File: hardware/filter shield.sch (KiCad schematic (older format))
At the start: 9 parts, among them J1 Screw_Terminal_01x03, J2 Screw_Terminal_01x03, J3 TR switch Connector, J6 Screw_Terminal_01x03, J7 Radioberry Connector, J8 BPF Connector, J9 LPF Connector, U1 BOB-12009

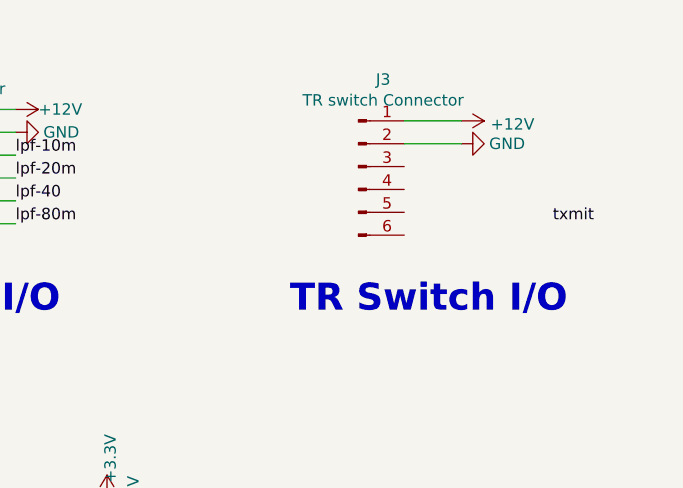
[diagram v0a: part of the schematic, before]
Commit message: tr switch circuit added
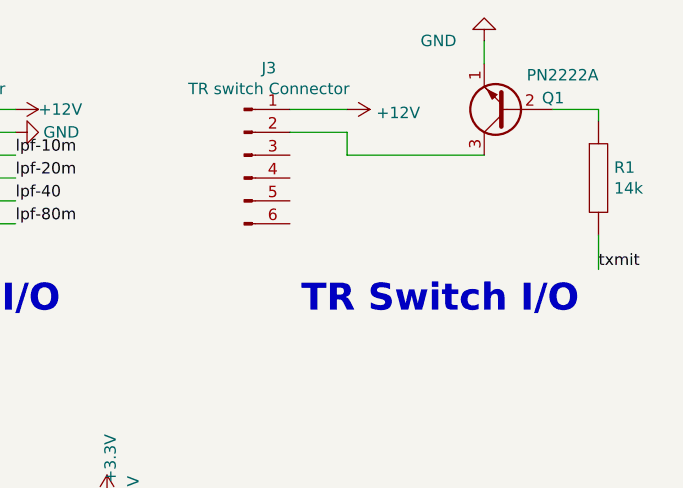
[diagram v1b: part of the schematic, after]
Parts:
- added Q1: PN2222A, Package_TO_SOT_THT:TO-92_Inline, symbol Transistor_BJT:PN2222A
- added R1: 14k, Resistor_THT:R_Axial_DIN0204_L3.6mm_D1.6mm_P7.62mm_Horizontal, symbol pspice:R
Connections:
- net GND: now also Q1.1 (E); no longer J3.2 (Pin_2)
- net txmit: now also R1.2
- new net: Q1.2 (B), R1.1
- new net: J3.2 (Pin_2), Q1.3 (C)
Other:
- moved on the sheet: J3
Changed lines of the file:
@@
 Text Label 5600 4100 0    50   ~ 0
 ptt
-Text Label 10300 1500 0    50   ~ 0
+Text Label 10500 1700 0    50   ~ 0
 txmit
 Text Label 5800 1050 0    50   ~ 0
@@
 L power:GND #PWR0129
 U 1 1 5E57ED2C
-P 9900 1150
-F 0 "#PWR0129" H 9900 900 50  0001 C CNN
-F 1 "GND" V 9900 950 50  0000 C CNN
-F 2 "" H 9900 1150 50  0001 C CNN
-F 3 "" H 9900 1150 50  0001 C CNN
-	1    9900 1150
-	0    -1   -1   0
+P 10000 700
+F 0 "#PWR0129" H 10000 450 50  0001 C CNN
+F 1 "GND" H 10200 700 50  0000 C CNN
+F 2 "" H 10000 700 50  0001 C CNN
+F 3 "" H 10000 700 50  0001 C CNN
+	1    10000 700
+	-1   0    0    1
 $EndComp
 Wire Wire Line
@@
 L power:+12V #PWR0103
 U 1 1 5E5083D9
-P 9900 1050
-F 0 "#PWR0103" H 9900 900 50  0001 C CNN
-F 1 "+12V" V 9915 1178 50  0000 L CNN
-F 2 "" H 9900 1050 50  0001 C CNN
-F 3 "" H 9900 1050 50  0001 C CNN
-	1    9900 1050
+P 9400 1000
+F 0 "#PWR0103" H 9400 850 50  0001 C CNN
+F 1 "+12V" V 9415 1128 50  0000 L CNN
+F 2 "" H 9400 1000 50  0001 C CNN
+F 3 "" H 9400 1000 50  0001 C CNN
+	1    9400 1000
 	0    1    1    0
 $EndComp
@@
 L Connector:Conn_01x06_Male J3
 U 1 1 5E5186BE
-P 9450 1250
-F 0 "J3" H 9558 1631 50  0000 C CNN
-F 1 "TR switch Connector" H 9558 1540 50  0000 C CNN
-F 2 "Connector_PinHeader_2.54mm:PinHeader_1x06_P2.54mm_Vertical" H 9450 1250 50  0001 C CNN
-F 3 "~" H 9450 1250 50  0001 C CNN
-	1    9450 1250
+P 8950 1200
+F 0 "J3" H 9058 1581 50  0000 C CNN
+F 1 "TR switch Connector" H 9058 1490 50  0000 C CNN
+F 2 "Connector_PinHeader_2.54mm:PinHeader_1x06_P2.54mm_Vertical" H 8950 1200 50  0001 C CNN
+F 3 "~" H 8950 1200 50  0001 C CNN
+	1    8950 1200
 	1    0    0    -1
 $EndComp
@@
 	5850 1550 5600 1550
 Wire Wire Line
-	9900 1050 9650 1050
-Wire Wire Line
-	9900 1150 9650 1150
+	9400 1000 9150 1000
+Wire Wire Line
+	9400 1100 9150 1100
 Text Notes 750  1900 0    118  ~ 24
 Power Inputs
@@
 Text Notes 7500 1900 0    118  ~ 24
 LPF I/O
-Text Notes 9150 1900 0    118  ~ 24
+Text Notes 9200 1900 0    118  ~ 24
 TR Switch I/O
 Text Notes 950  4500 0    118  ~ 24
@@
 Wire Wire Line
 	7750 4150 7400 4150
+$Comp
+L pspice:R R1
+U 1 1 5E4E14AD
+P 10500 1300
+F 0 "R1" H 10568 1346 50  0000 L CNN
+F 1 "14k" H 10568 1255 50  0000 L CNN
+F 2 "Resistor_THT:R_Axial_DIN0204_L3.6mm_D1.6mm_P7.62mm_Horizontal" H 10500 1300 50  0001 C CNN
+F 3 "~" H 10500 1300 50  0001 C CNN
+	1    10500 1300
+	1    0    0    -1
+$EndComp
+$Comp
+L Transistor_BJT:PN2222A Q1
+U 1 1 5E4E27AE
+P 10100 1000
+F 0 "Q1" H 9850 950 50  0000 L CNN
+F 1 "PN2222A" H 9700 850 50  0000 L CNN
+F 2 "Package_TO_SOT_THT:TO-92_Inline" H 10300 925 50  0001 L CIN
+F 3 "http://www.fairchildsemi.com/ds/PN/PN2222A.pdf" H 10100 1000 50  0001 L CNN
+	1    10100 1000
+	-1   0    0    1
+$EndComp
+Wire Wire Line
+	10000 700  10000 800
+Wire Wire Line
+	10500 1050 10500 1000
+Wire Wire Line
+	10500 1000 10300 1000
+Wire Wire Line
+	10500 1700 10500 1550
+Wire Wire Line
+	10000 1200 9400 1200
+Wire Wire Line
+	9400 1200 9400 1100
 $EndSCHEMATC

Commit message: Small corrections
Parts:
- added Q2: PN2222A, Package_TO_SOT_THT:TO-92_Inline, symbol Transistor_BJT:PN2222A
- added R2: 14k, Resistor_THT:R_Axial_DIN0204_L3.6mm_D1.6mm_P7.62mm_Horizontal, symbol pspice:R
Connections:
- net GND: now also J3.3 (Pin_3), J3.5 (Pin_5), Q2.1 (E)
- net pa: now reaches A1.9 (D6)
- net pa: now also R2.2
- net at J3.4 (Pin_4): now also Q2.3 (C)
- new net: Q2.2 (B), R2.1
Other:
- note added: "TR Switch-PA I/O"
- note removed: "TR Switch I/O"
- moved on the sheet: R1
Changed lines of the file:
@@
 Text Label 5600 4100 0    50   ~ 0
 ptt
-Text Label 10500 1700 0    50   ~ 0
+Text Label 10800 1000 0    50   ~ 0
 txmit
 Text Label 5800 1050 0    50   ~ 0
@@
 Text Notes 7500 1900 0    118  ~ 24
 LPF I/O
-Text Notes 9200 1900 0    118  ~ 24
-TR Switch I/O
+Text Notes 9200 2200 0    118  ~ 24
+TR Switch-PA I/O
 Text Notes 950  4500 0    118  ~ 24
 PA power
@@
 L pspice:R R1
 U 1 1 5E4E14AD
-P 10500 1300
-F 0 "R1" H 10568 1346 50  0000 L CNN
-F 1 "14k" H 10568 1255 50  0000 L CNN
-F 2 "Resistor_THT:R_Axial_DIN0204_L3.6mm_D1.6mm_P7.62mm_Horizontal" H 10500 1300 50  0001 C CNN
-F 3 "~" H 10500 1300 50  0001 C CNN
-	1    10500 1300
-	1    0    0    -1
+P 10550 1000
+F 0 "R1" H 10618 1046 50  0000 L CNN
+F 1 "14k" H 10618 955 50  0000 L CNN
+F 2 "Resistor_THT:R_Axial_DIN0204_L3.6mm_D1.6mm_P7.62mm_Horizontal" H 10550 1000 50  0001 C CNN
+F 3 "~" H 10550 1000 50  0001 C CNN
+	1    10550 1000
+	0    -1   -1   0
 $EndComp
 $Comp
@@
 	10000 700  10000 800
 Wire Wire Line
-	10500 1050 10500 1000
-Wire Wire Line
-	10500 1000 10300 1000
-Wire Wire Line
-	10500 1700 10500 1550
-Wire Wire Line
 	10000 1200 9400 1200
 Wire Wire Line
 	9400 1200 9400 1100
+$Comp
+L power:GND #PWR0120
+U 1 1 5E50D80E
+P 10000 1350
+F 0 "#PWR0120" H 10000 1100 50  0001 C CNN
+F 1 "GND" H 10200 1350 50  0000 C CNN
+F 2 "" H 10000 1350 50  0001 C CNN
+F 3 "" H 10000 1350 50  0001 C CNN
+	1    10000 1350
+	-1   0    0    1
+$EndComp
+$Comp
+L pspice:R R2
+U 1 1 5E50D819
+P 10550 1650
+F 0 "R2" H 10618 1696 50  0000 L CNN
+F 1 "14k" H 10618 1605 50  0000 L CNN
+F 2 "Resistor_THT:R_Axial_DIN0204_L3.6mm_D1.6mm_P7.62mm_Horizontal" H 10550 1650 50  0001 C CNN
+F 3 "~" H 10550 1650 50  0001 C CNN
+	1    10550 1650
+	0    -1   -1   0
+$EndComp
+$Comp
+L Transistor_BJT:PN2222A Q2
+U 1 1 5E50D823
+P 10100 1650
+F 0 "Q2" H 9850 1600 50  0000 L CNN
+F 1 "PN2222A" H 9700 1500 50  0000 L CNN
+F 2 "Package_TO_SOT_THT:TO-92_Inline" H 10300 1575 50  0001 L CIN
+F 3 "http://www.fairchildsemi.com/ds/PN/PN2222A.pdf" H 10100 1650 50  0001 L CNN
+	1    10100 1650
+	-1   0    0    1
+$EndComp
+Wire Wire Line
+	10000 1350 10000 1450
+Wire Wire Line
+	10000 1850 9400 1850
+Text Label 7400 4050 0    50   ~ 0
+pa
+Text Label 10800 1650 0    50   ~ 0
+pa
+Wire Wire Line
+	7400 4050 7750 4050
+Wire Wire Line
+	9400 1850 9400 1300
+Wire Wire Line
+	9400 1300 9150 1300
+$Comp
+L power:GND #PWR0121
+U 1 1 5E53E548
+P 9150 1400
+F 0 "#PWR0121" H 9150 1150 50  0001 C CNN
+F 1 "GND" V 9150 1200 50  0000 C CNN
+F 2 "" H 9150 1400 50  0001 C CNN
+F 3 "" H 9150 1400 50  0001 C CNN
+	1    9150 1400
+	0    -1   -1   0
+$EndComp
+$Comp
+L power:GND #PWR0122
+U 1 1 5E540C7C
+P 9150 1200
+F 0 "#PWR0122" H 9150 950 50  0001 C CNN
+F 1 "GND" V 9150 1000 50  0000 C CNN
+F 2 "" H 9150 1200 50  0001 C CNN
+F 3 "" H 9150 1200 50  0001 C CNN
+	1    9150 1200
+	0    -1   -1   0
+$EndComp
 $EndSCHEMATC

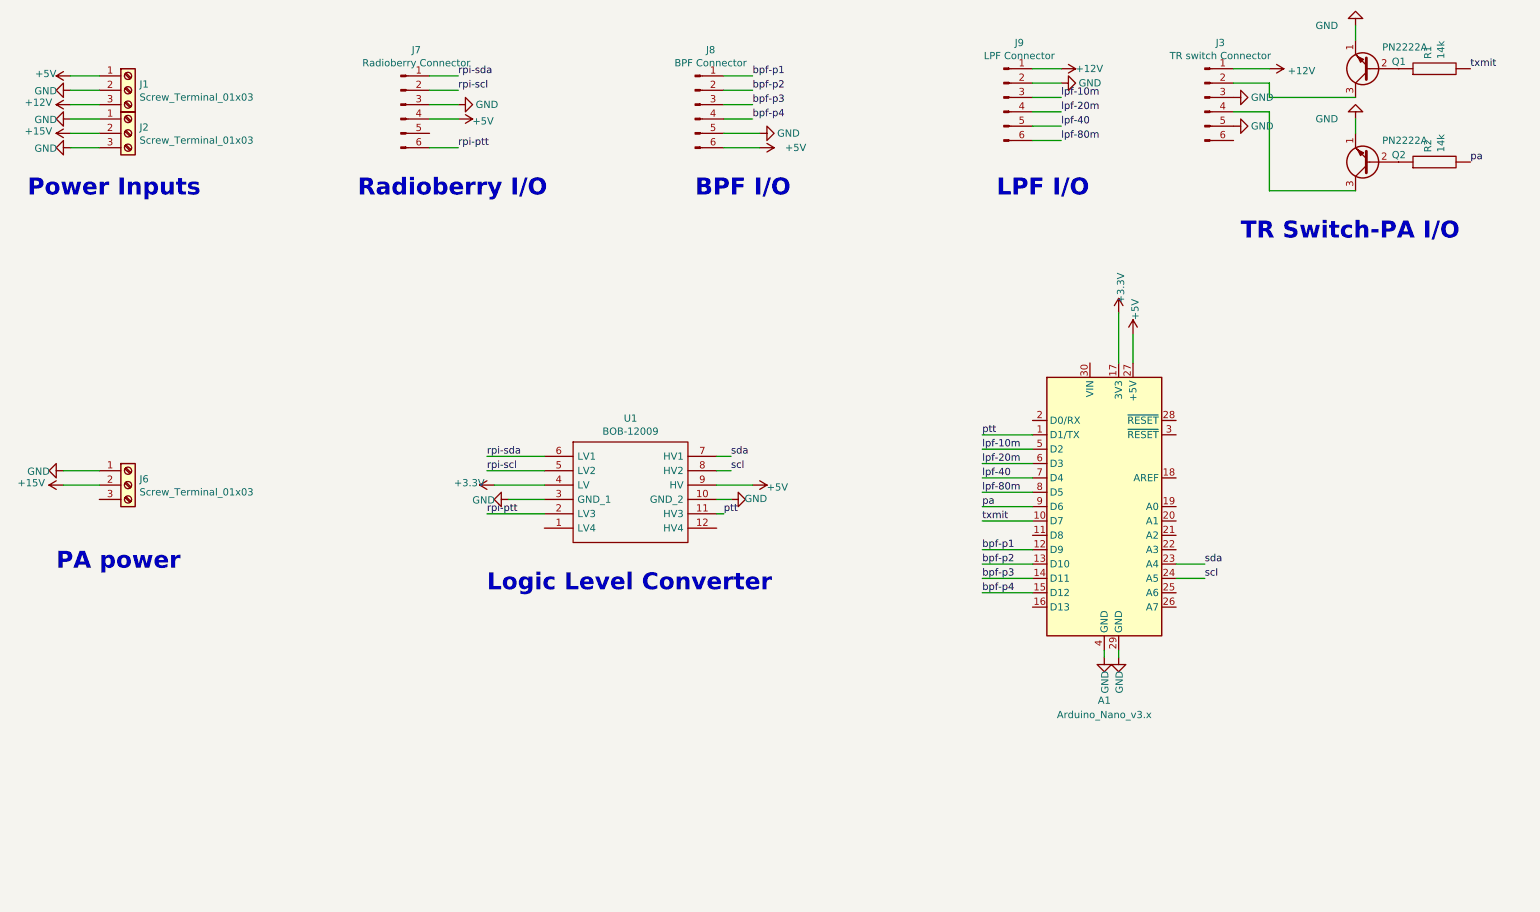
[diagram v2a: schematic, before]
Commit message: Revised circuit to meet lpf protocol. Added futur expansion i/o over analog pins
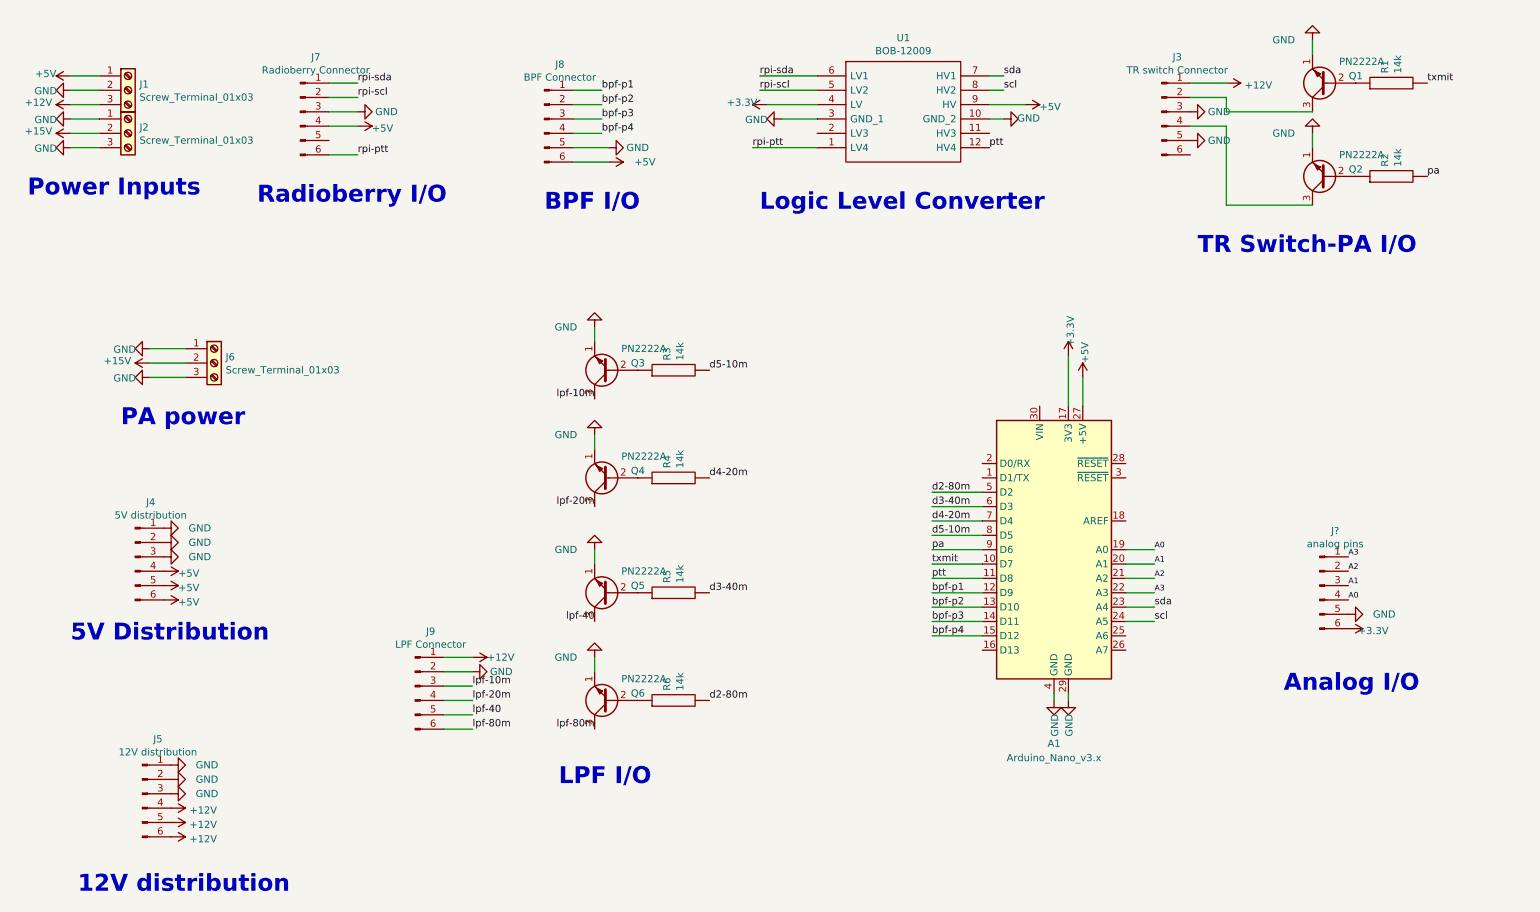
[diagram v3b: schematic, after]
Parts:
- added J4: 5V distribution, Connector_PinHeader_2.54mm:PinHeader_1x06_P2.54mm_Vertical, symbol Connector:Conn_01x06_Male
- added J5: 12V distribution, Connector_PinHeader_2.54mm:PinHeader_1x06_P2.54mm_Vertical, symbol Connector:Conn_01x06_Male
- added J?: analog pins, Connector_PinHeader_2.54mm:PinHeader_1x06_P2.54mm_Vertical, symbol Connector:Conn_01x06_Male
- added Q3, Q4, Q5, Q6: PN2222A, Package_TO_SOT_THT:TO-92_Inline, symbol Transistor_BJT:PN2222A
- added R3, R4, R5, R6: 14k, Resistor_THT:R_Axial_DIN0204_L3.6mm_D1.6mm_P7.62mm_Horizontal, symbol pspice:R
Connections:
- net +12V: now also J5.4 (Pin_4), J5.5 (Pin_5), J5.6 (Pin_6)
- net +3V3: now also J?.6 (Pin_6)
- net +5V: now also J4.4 (Pin_4), J4.5 (Pin_5), J4.6 (Pin_6)
- net GND: now also J6.3 (Pin_3), J4.1 (Pin_1), J4.2 (Pin_2), J4.3 (Pin_3), J5.1 (Pin_1), J5.2 (Pin_2), J5.3 (Pin_3), J?.5 (Pin_5), Q3.1 (E), Q4.1 (E), Q5.1 (E), Q6.1 (E)
- net lpf-10m: now also Q3.3 (C); no longer A1.5 (D2)
- net lpf-20m: now also Q4.3 (C); no longer A1.6 (D3)
- net lpf-40: now also Q5.3 (C); no longer A1.7 (D4)
- net lpf-80m: now also Q6.3 (C); no longer A1.8 (D5)
- net ptt: now also A1.11 (D8), U1.12 (HV4); no longer A1.1 (D1/TX), U1.11 (HV3)
- net rpi-ptt: now also U1.1 (LV4); no longer U1.2 (LV3)
- net A0: now reaches A1.19 (A0)
- net A0: now also J?.4 (Pin_4)
- net A1: now reaches A1.20 (A1)
- net A1: now also J?.3 (Pin_3)
- net A2: now reaches A1.21 (A2)
- net A2: now also J?.2 (Pin_2)
- net A3: now reaches A1.22 (A3)
- net A3: now also J?.1 (Pin_1)
- new net: Q3.2 (B), R3.1
- new net: Q4.2 (B), R4.1
- new net: Q5.2 (B), R5.1
- new net: Q6.2 (B), R6.1
- new net d2-80m: A1.5 (D2), R6.2
- new net d3-40m: A1.6 (D3), R5.2
- new net d4-20m: A1.7 (D4), R4.2
- new net d5-10m: A1.8 (D5), R3.2
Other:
- note added: "12V distribution"
- note added: "5V Distribution"
- note added: "Analog I/O"
- moved on the sheet: A1, J3, J6, J7, J8, J9, Q1, Q2, R1, R2, U1

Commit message: Small changes
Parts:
- gave numbers to parts that had none: 1
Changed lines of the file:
@@
 	1600 3150 1850 3150
 $Comp
-L Connector:Conn_01x06_Male J?
+L Connector:Conn_01x06_Male J10
 U 1 1 5E5DAB43
 P 9750 4600
-F 0 "J?" H 9858 4981 50  0000 C CNN
+F 0 "J10" H 9858 4981 50  0000 C CNN
 F 1 "analog pins" H 9858 4890 50  0000 C CNN
 F 2 "Connector_PinHeader_2.54mm:PinHeader_1x06_P2.54mm_Vertical" H 9750 4600 50  0001 C CNN
@@
 $EndComp
 $Comp
-L power:GND #PWR?
+L power:GND #PWR0145
 U 1 1 5E5DAB57
 P 9950 4800
-F 0 "#PWR?" H 9950 4550 50  0001 C CNN
+F 0 "#PWR0145" H 9950 4550 50  0001 C CNN
 F 1 "GND" V 9950 4550 50  0000 C CNN
 F 2 "" H 9950 4800 50  0001 C CNN
@@
 $EndComp
 $Comp
-L power:+3.3V #PWR?
+L power:+3.3V #PWR0146
 U 1 1 5E5F32A6
 P 9950 4900
-F 0 "#PWR?" H 9950 4750 50  0001 C CNN
+F 0 "#PWR0146" H 9950 4750 50  0001 C CNN
 F 1 "+3.3V" V 9965 5073 50  0000 C CNN
 F 2 "" H 9950 4900 50  0001 C CNN

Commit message: Change screw terminal to 5mm footprint
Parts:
- J1, J2, J6: footprint TerminalBlock_4Ucon:TerminalBlock_4Ucon_1x03_P3.50mm_Horizontal -> TerminalBlock:TerminalBlock_Altech_AK300-3_P5.00mm
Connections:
- net +12V: now also J1.1 (Pin_1); no longer J1.3 (Pin_3)
- net +5V: now also J1.3 (Pin_3); no longer J1.1 (Pin_1)
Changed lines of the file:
@@
 encoding utf-8
 Sheet 1 1
-Title "Radioberry Generic Filters Boards interface. "
+Title "Radioberry Companion Board interface. "
 Date "mar. 31 mars 2015"
-Rev "0.1"
+Rev "0.2"
 Comp "VA2SAJ"
 Comment1 ""
@@
 F 0 "J1" H 1530 1192 50  0000 L CNN
 F 1 "Screw_Terminal_01x03" H 1530 1101 50  0000 L CNN
-F 2 "TerminalBlock_4Ucon:TerminalBlock_4Ucon_1x03_P3.50mm_Horizontal" H 1450 1150 50  0001 C CNN
+F 2 "TerminalBlock:TerminalBlock_Altech_AK300-3_P5.00mm" H 1450 1150 50  0001 C CNN
 F 3 "~" H 1450 1150 50  0001 C CNN
 	1    1450 1150
@@
 F 0 "J2" H 1530 1492 50  0000 L CNN
 F 1 "Screw_Terminal_01x03" H 1530 1401 50  0000 L CNN
-F 2 "TerminalBlock_4Ucon:TerminalBlock_4Ucon_1x03_P3.50mm_Horizontal" H 1450 1450 50  0001 C CNN
+F 2 "TerminalBlock:TerminalBlock_Altech_AK300-3_P5.00mm" H 1450 1450 50  0001 C CNN
 F 3 "~" H 1450 1450 50  0001 C CNN
 	1    1450 1450
@@
 F 0 "J6" H 2130 3092 50  0000 L CNN
 F 1 "Screw_Terminal_01x03" H 2130 3001 50  0000 L CNN
-F 2 "TerminalBlock_4Ucon:TerminalBlock_4Ucon_1x03_P3.50mm_Horizontal" H 2050 3050 50  0001 C CNN
+F 2 "TerminalBlock:TerminalBlock_Altech_AK300-3_P5.00mm" H 2050 3050 50  0001 C CNN
 F 3 "~" H 2050 3050 50  0001 C CNN
 	1    2050 3050
@@
 L power:+5V #PWR0101
 U 1 1 5E4CACAA
-P 1050 1050
-F 0 "#PWR0101" H 1050 900 50  0001 C CNN
-F 1 "+5V" V 1065 1223 50  0000 C CNN
-F 2 "" H 1050 1050 50  0001 C CNN
-F 3 "" H 1050 1050 50  0001 C CNN
-	1    1050 1050
+P 1050 1250
+F 0 "#PWR0101" H 1050 1100 50  0001 C CNN
+F 1 "+5V" V 1050 1450 50  0000 C CNN
+F 2 "" H 1050 1250 50  0001 C CNN
+F 3 "" H 1050 1250 50  0001 C CNN
+	1    1050 1250
 	0    -1   -1   0
 $EndComp
@@
 L power:+12V #PWR0106
 U 1 1 5E50A141
-P 1050 1250
-F 0 "#PWR0106" H 1050 1100 50  0001 C CNN
-F 1 "+12V" V 1065 1378 50  0000 L CNN
-F 2 "" H 1050 1250 50  0001 C CNN
-F 3 "" H 1050 1250 50  0001 C CNN
-	1    1050 1250
+P 1050 1050
+F 0 "#PWR0106" H 1050 900 50  0001 C CNN
+F 1 "+12V" V 1065 1178 50  0000 L CNN
+F 2 "" H 1050 1050 50  0001 C CNN
+F 3 "" H 1050 1050 50  0001 C CNN
+	1    1050 1050
 	0    -1   -1   0
 $EndComp
